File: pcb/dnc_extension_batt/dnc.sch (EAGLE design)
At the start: 49 parts, among them Q1 IRF9321PBF, Q2 IRF9321PBF, Q5 BSS138

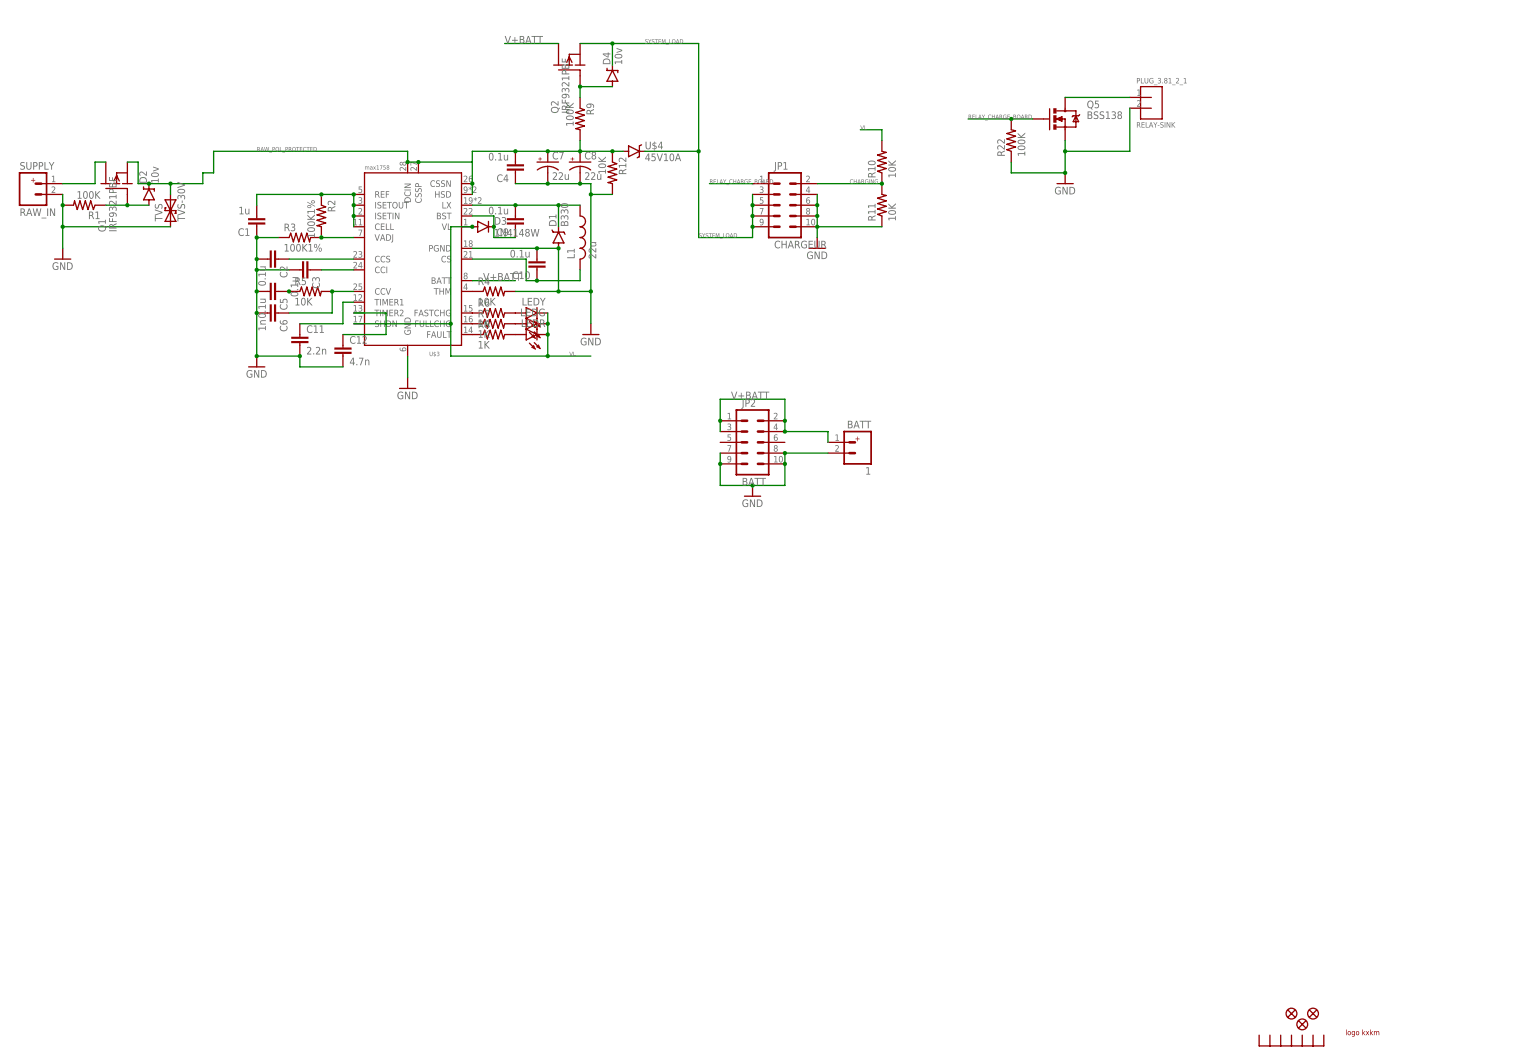
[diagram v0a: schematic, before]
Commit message: add remote + enclosure
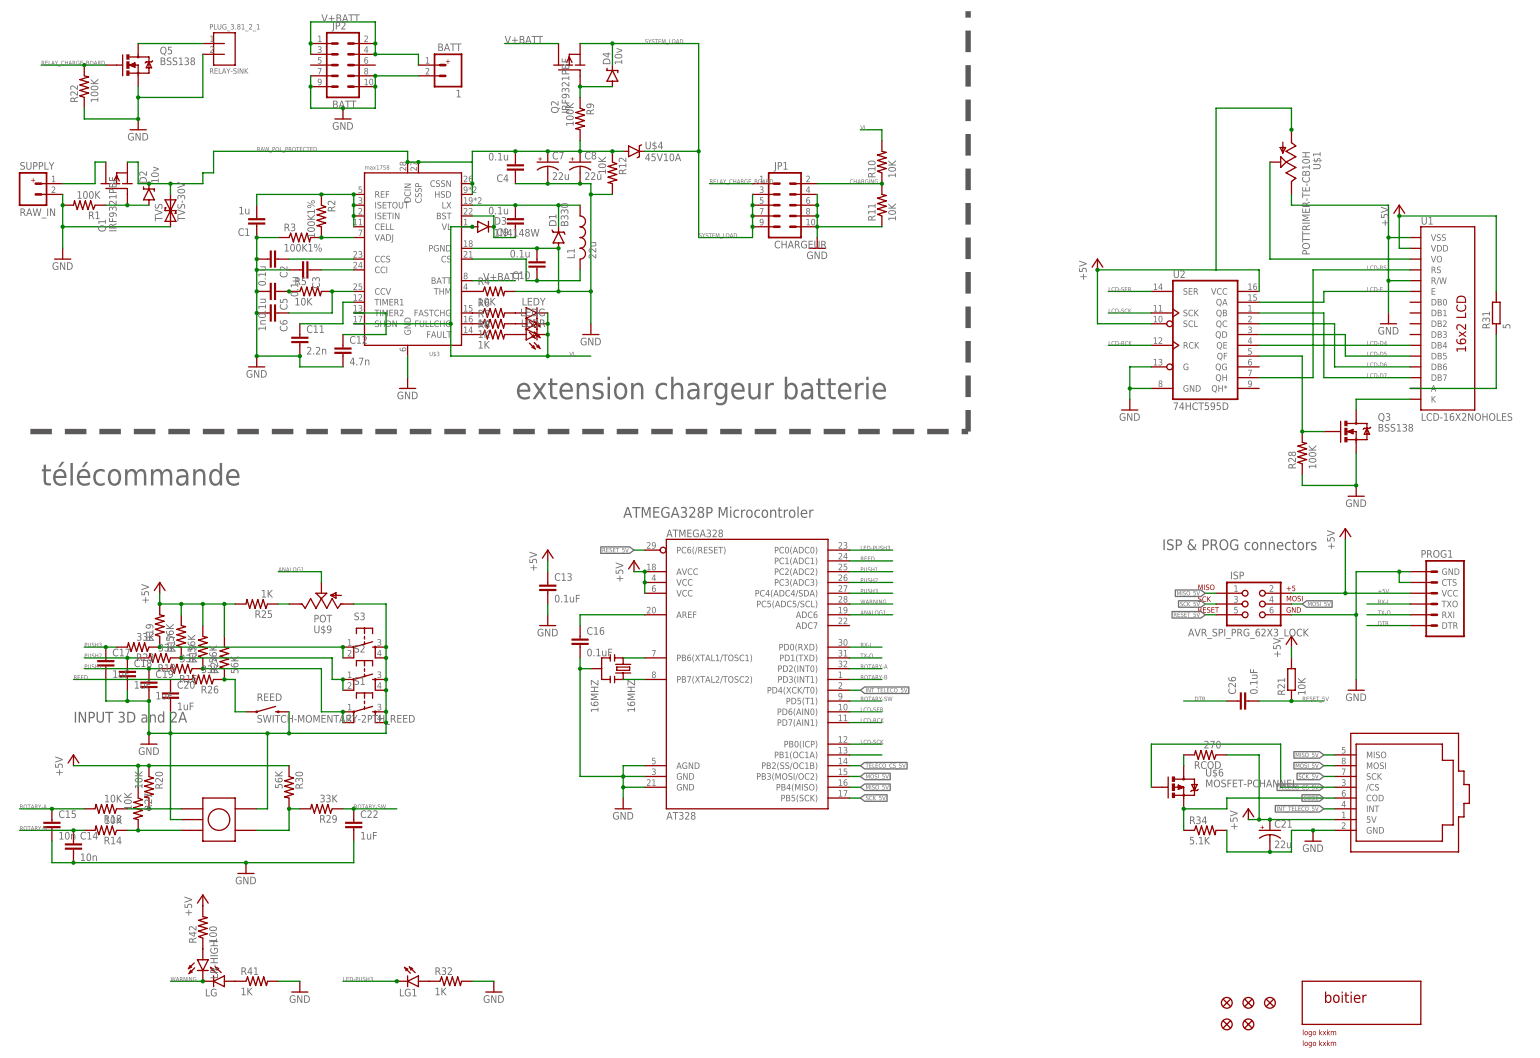
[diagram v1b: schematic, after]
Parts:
- added 16MHZ: 16MHZ, SparkFun-FreqCtrl:RESONATOR16MHZ
- added AT328: ATMEGA328, SparkFun:ATMEGA168
- added C13, C16, C26: 0.1uF, rcl:C-EUC0603
- added C14, C15: 10n, rcl:C-EUC0603
- added C17, C18, C19, C20, C22: 1uF, rcl:C-EUC0603
- added C21: 22u, SparkFun-Passives:CAP_POL1206
- added ISP: AVR_SPI_PRG_62X3_LOCK, SparkFun:AVR_SPI_PRG_62X3_LOCK
- added JP3, JP4: FIDUCIAL1X2.5, SparkFun:FIDUCIAL1X2.5
- added LG, LG1, LR-HIGH: (no value), SparkFun-LED:LED1206
- added PROG1: (no value), SparkFun:ARDUINO_SERIAL_PROGRAMLOCK
- added Q3: BSS138, SparkFun-DiscreteSemi:MOSFET-NCHANNELBSS138
- added R13, R14, R20, R27: 10K, SparkFun-Passives:RESISTOR0603-RES
- added R15, R17, R19, R24, R30: 56K, SparkFun-Passives:RESISTOR0603-RES
- added R16, R18, R23, R26, R29: 33K, SparkFun-Passives:RESISTOR0603-RES
- added R21: 10K, rcl:R-EU_R0603
- added R25, R32, R41: 1K, SparkFun-Passives:RESISTOR0603-RES
- added R28: 100K, SparkFun-Passives:RESISTOR0603-RES
- added R31: 5, rcl:R-EU_R0603
- added R34: 5.1K, SparkFun-Passives:RESISTOR0603-RES
- added R42: 100, SparkFun-Passives:RESISTOR0603-RES
- added RCOD: 270, SparkFun-Passives:RESISTOR0603-RES
- added REED: SWITCH-MOMENTARY-2PTH_REED, SparkFun-Electromechanical:SWITCH-MOMENTARY-2PTH_REED
- added S1, S2, S3: (no value), SparkFun:TAC_SWITCHPTH
- added U$5: BOITIERBOITIER_FARNELLE_479-0020-0, pierre_vv:BOITIERBOITIER_FARNELLE_479-0020-0
- added U$6: MOSFET-PCHANNEL, SparkFun-DiscreteSemi:MOSFET-PCHANNEL
- added U$6MOV: LOGO, pierre_vv:LOGO
- added U$7: ROTARYEC12D1564404, pierre_vv:ROTARYEC12D1564404
- added U$8: RJ45-EXTDNC, con-amphenol-rj45-ld:RJ45-EXTDNC
- added U$9: POT, pierre_vv:POT
- added U1: LCD-16X2NOHOLES, SparkFun-Displays:LCD-16X2NOHOLES
- added U2: 74HCT595D, IC:74HCT595D
- U$1: value RADIATEUR -> POTTRIMER-TE-CB10H; device pierre_vv:RADIATEUR -> pierre_vv:POTTRIMER-TE-CB10H
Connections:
- new net +5V: AT328.AVCC, AT328.VCC@1, AT328.VCC@2, C13.1, C21.+, ISP.2, PROG1.VCC, R15.2, R17.2, R19.2, R20.1, R21.2, R24.2, R25.2, R27.1, R30.1, R31.2, R42.2, RCOD.1, U$1.A, U$8.5V, U1.VDD, U2.SCL, U2.VCC
- new net ANALOG1: AT328.ADC6, U$9.S
- new net AREF: AT328.AREF, C16.1
- new net CODE: R34.1, U$6.S, U$8.COD
- new net DTR: C26.1, PROG1.DTR
- new net INT_TELECO_5V: AT328.PD4(XCK/T0), U$8.INT
- new net LCD-D4: U1.DB4, U2.QE
- new net LCD-D5: U1.DB5, U2.QD
- new net LCD-D6: U1.DB6, U2.QC
- new net LCD-D7: U1.DB7, U2.QB
- new net LCD-E: U1.E, U2.QA
- new net LCD-LED-CONTROL: Q3.G, R28.2, U2.QF
- new net LCD-RCK: AT328.PD7(AIN1), U2.RCK
- new net LCD-RS: U1.RS, U2.QH
- new net LCD-SCK: AT328.PB0(ICP), U2.SCK
- new net LCD-SER: AT328.PD6(AIN0), U2.SER
- new net LED-PUSH3: AT328.PC0(ADC0), LG1.C
- new net MISO_5V: AT328.PB4(MISO), ISP.1, U$8.MISO
- new net MOSI_5V: AT328.PB3(MOSI/OC2), ISP.4, U$8.MOSI
- new net N$22: R15.1, R16.1, S1.1, S1.2
- new net N$23: R14.1, R27.2, U$7.A
- new net N$24: R17.1, R18.1, S2.1, S2.2
- new net N$25: R13.1, R20.2, U$7.B
- new net N$26: R19.1, R23.1, S3.1, S3.2
- new net N$27: R25.1, U$9.E
- new net N$28: R24.1, R26.1, REED.1
- new net N$29: LR-HIGH.A, R42.1
- new net N$30: LG.A, R41.1
- new net N$31: R29.2, R30.2, U$7.SW2
- new net N$32: R31.1, U1.A
- new net N$33: U$1.S, U1.VO
- new net N$34: Q3.D, U1.K
- new net N$35: LG1.A, R32.1
- new net N$36: RCOD.2, U$6.D
- new net N$38: AT328.PB1(OC1A)
- new net N$43: 16MHZ.1, AT328.PB6(XTAL1/TOSC1)
- new net N$44: 16MHZ.3, AT328.PB7(XTAL2/TOSC2)
- new net PUSH1: AT328.PC2(ADC2), C19.1, R16.2
- new net PUSH2: AT328.PC3(ADC3), C18.1, R18.2
- new net PUSH3: AT328.PC4(ADC4/SDA), C17.1, R23.2
- new net REED: AT328.PC1(ADC1), C20.1, R26.2
- new net RESET_5V: AT328.PC6(/RESET), C26.2, ISP.5, R21.1
- new net ROTARY-A: AT328.PD2(INT0), C15.1, R13.2
- new net ROTARY-B: AT328.PD3(INT1), C14.1, R14.2
- new net ROTARY-SW: AT328.PD5(T1), C22.1, R29.1
- new net RX-I: AT328.PD0(RXD), PROG1.TXO
- new net SCK_5V: AT328.PB5(SCK), ISP.3, U$8.SCK
- new net TELECO_CS_5V: AT328.PB2(SS/OC1B), U$6.G, U$8./CS
- new net TX-O: AT328.PD1(TXD), PROG1.RXI
- new net WARNING: AT328.PC5(ADC5/SCL), LG.C, LR-HIGH.C
- net GND: now also 16MHZ.2, AT328.AGND, AT328.GND@1, AT328.GND@2, C13.2, C14.2, C15.2, C16.2, C17.2, C18.2, C19.2, C20.2, C21.-, C22.2, ISP.6, PROG1.CTS, PROG1.GND, Q3.S, R28.1, R32.2, R34.2, R41.2, REED.2, S1.3, S1.4, S2.3, S2.4, S3.3, S3.4, U$1.E, U$7.COM, U$7.SW1, U$8.GND, U$9.A, U1.R/W, U1.VSS, U2.G, U2.GND
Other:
- note added: "ATMEGA328P Microcontroler"
- note added: "CS titreur driver"
- note added: "INPUT 3D and 2A"
- note added: "ISP & PROG connectors"
- note added: "extension chargeur batterie"
- note added: "télécommande"
- moved on the sheet: 1, JP2, PLUG_3.81_2_1, Q5, R22

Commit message: BOM ext teleco et chargeur
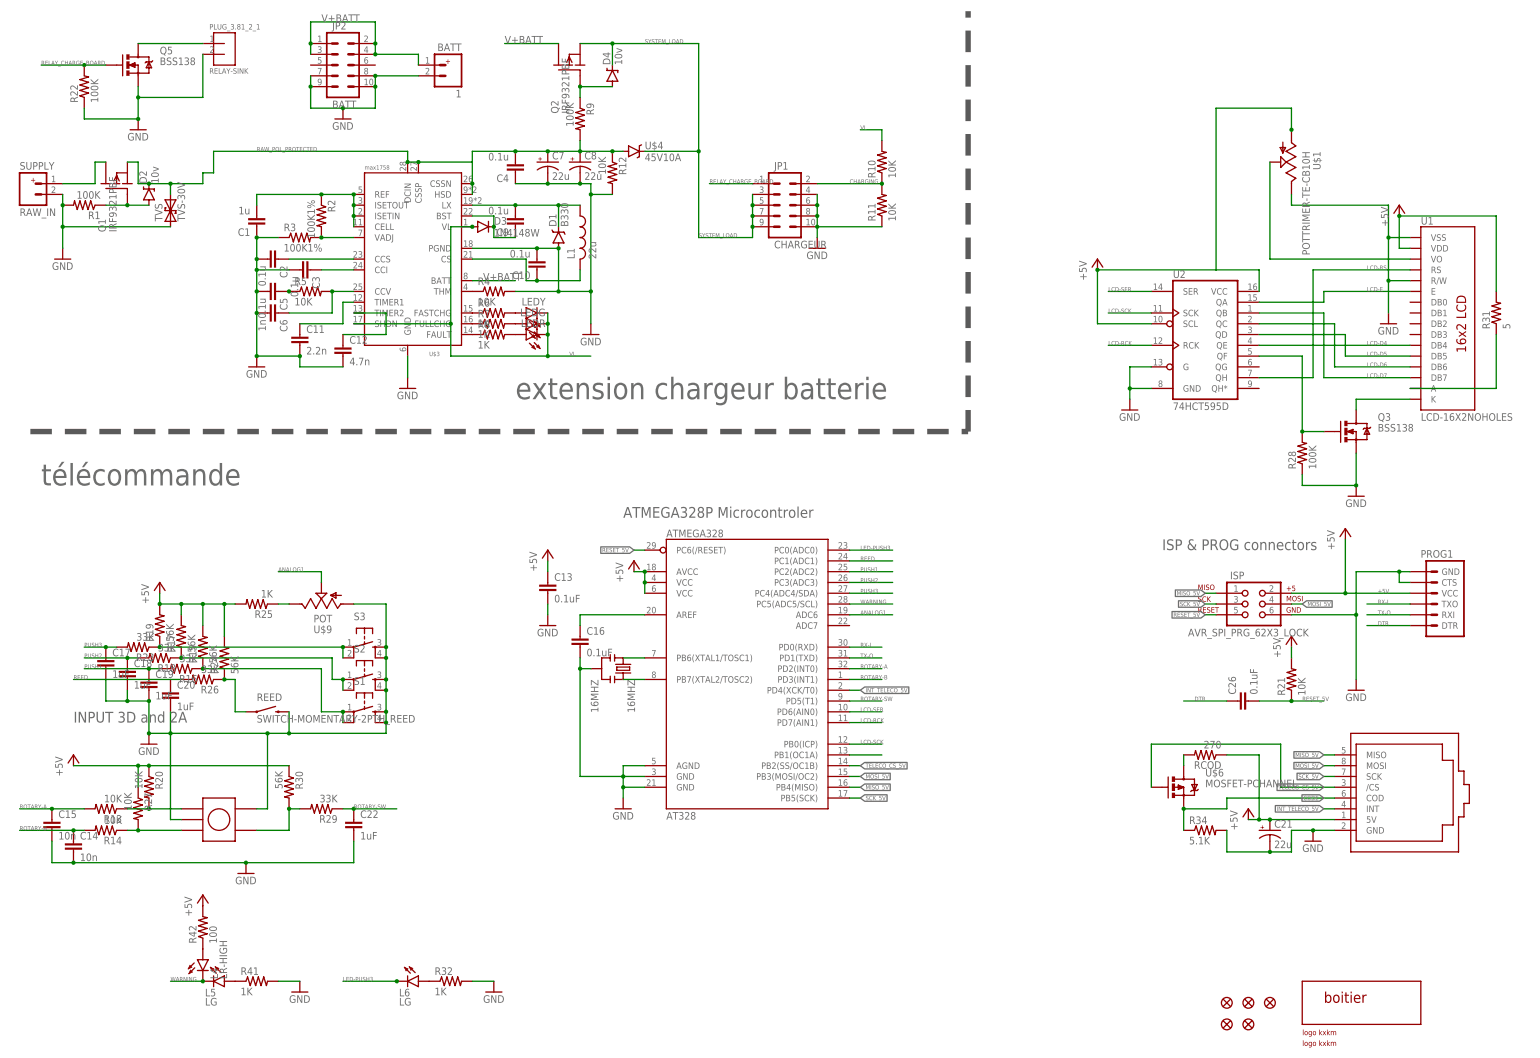
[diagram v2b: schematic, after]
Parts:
- 1, C1, C11, C12, C2, C3, C5, C6, D1, D2, D3, D4, JP1, JP2, L1, LEDG, LEDR, LEDY, PLUG_3.81_2_1, Q1, Q2, Q5, R1, R10, R11, R12, R2, R22, R3, R4, R5, R6, R7, R8, R9, RAW_IN, TVS, U$3, U$4: C (none) -> 1
- C10, C4, C7, C8, C9: C (none) -> 1; VMIN (none) -> 35V
- L4: value (none) -> LR-HIGH
- L5, L6: value (none) -> LG
- R21: device rcl:R-EU_R0603 -> SparkFun-Passives:RESISTOR0603-RES
- R31: device rcl:R-EU_R0603 -> SparkFun-Passives:RESISTOR0805-RES; P (none) -> 250mw
- renumbered LG to L5, LG1 to L6, LR-HIGH to L4

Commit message: major change correction : - driver led position - add usb for power - correct max 202 voltage problem - titrer connector position - forget line - power trace consideration
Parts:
- JP1: device SparkFun:M05X2SHD_LOCK -> pierre_vv:M05X2
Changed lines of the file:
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@@
 <grid distance="0.1" unitdist="inch" unit="inch" style="lines" multiple="1" display="no" altdistance="0.01" altunitdist="inch" altunit="inch"/>
 <layers>
-<layer number="1" name="Top" color="4" fill="1" visible="yes" active="no"/>
-<layer number="16" name="Bottom" color="1" fill="1" visible="yes" active="no"/>
-<layer number="17" name="Pads" color="2" fill="1" visible="yes" active="no"/>
-<layer number="18" name="Vias" color="2" fill="1" visible="yes" active="no"/>
-<layer number="19" name="Unrouted" color="13" fill="1" visible="yes" active="no"/>
-<layer number="20" name="Dimension" color="15" fill="1" visible="yes" active="no"/>
-<layer number="21" name="tPlace" color="7" fill="1" visible="yes" active="no"/>
-<layer number="22" name="bPlace" color="7" fill="1" visible="yes" active="no"/>
-<layer number="23" name="tOrigins" color="15" fill="1" visible="yes" active="no"/>
-<layer number="24" name="bOrigins" color="15" fill="1" visible="yes" active="no"/>
-<layer number="25" name="tNames" color="7" fill="1" visible="yes" active="no"/>
-<layer number="26" name="bNames" color="7" fill="1" visible="yes" active="no"/>
-<layer number="27" name="tValues" color="7" fill="1" visible="yes" active="no"/>
-<layer number="28" name="bValues" color="7" fill="1" visible="yes" active="no"/>
+<layer number="1" name="Top" color="4" fill="1" visible="no" active="no"/>
+<layer number="16" name="Bottom" color="1" fill="1" visible="no" active="no"/>
+<layer number="17" name="Pads" color="2" fill="1" visible="no" active="no"/>
+<layer number="18" name="Vias" color="2" fill="1" visible="no" active="no"/>
+<layer number="19" name="Unrouted" color="13" fill="1" visible="no" active="no"/>
+<layer number="20" name="Dimension" color="15" fill="1" visible="no" active="no"/>
+<layer number="21" name="tPlace" color="7" fill="1" visible="no" active="no"/>
+<layer number="22" name="bPlace" color="7" fill="1" visible="no" active="no"/>
+<layer number="23" name="tOrigins" color="15" fill="1" visible="no" active="no"/>
+<layer number="24" name="bOrigins" color="15" fill="1" visible="no" active="no"/>
+<layer number="25" name="tNames" color="7" fill="1" visible="no" active="no"/>
+<layer number="26" name="bNames" color="7" fill="1" visible="no" active="no"/>
+<layer number="27" name="tValues" color="7" fill="1" visible="no" active="no"/>
+<layer number="28" name="bValues" color="7" fill="1" visible="no" active="no"/>
 <layer number="29" name="tStop" color="7" fill="3" visible="no" active="no"/>
 <layer number="30" name="bStop" color="7" fill="6" visible="no" active="no"/>
@@
 <layer number="35" name="tGlue" color="7" fill="4" visible="no" active="no"/>
 <layer number="36" name="bGlue" color="7" fill="5" visible="no" active="no"/>
-<layer number="37" name="tTest" color="7" fill="1" visible="yes" active="no"/>
-<layer number="38" name="bTest" color="7" fill="1" visible="yes" active="no"/>
+<layer number="37" name="tTest" color="7" fill="1" visible="no" active="no"/>
+<layer number="38" name="bTest" color="7" fill="1" visible="no" active="no"/>
 <layer number="39" name="tKeepout" color="4" fill="11" visible="no" active="no"/>
 <layer number="40" name="bKeepout" color="1" fill="11" visible="no" active="no"/>
@@
 <layer number="44" name="Drills" color="7" fill="1" visible="no" active="no"/>
 <layer number="45" name="Holes" color="7" fill="1" visible="no" active="no"/>
-<layer number="46" name="Milling" color="3" fill="1" visible="yes" active="no"/>
-<layer number="47" name="Measures" color="7" fill="1" visible="yes" active="no"/>
-<layer number="48" name="Document" color="7" fill="1" visible="yes" active="no"/>
-<layer number="49" name="Reference" color="7" fill="1" visible="yes" active="no"/>
-<layer number="50" name="dxf" color="7" fill="1" visible="yes" active="no"/>
-<layer number="51" name="tDocu" color="14" fill="1" visible="yes" active="no"/>
-<layer number="52" name="bDocu" color="14" fill="1" visible="yes" active="no"/>
-<layer number="53" name="tGND_GNDA" color="7" fill="9" visible="yes" active="no"/>
-<layer number="54" name="bGND_GNDA" color="1" fill="9" visible="yes" active="no"/>
-<layer number="56" name="wert" color="7" fill="1" visible="yes" active="no"/>
-<layer number="57" name="tCAD" color="7" fill="1" visible="yes" active="no"/>
+<layer number="46" name="Milling" color="3" fill="1" visible="no" active="no"/>
+<layer number="47" name="Measures" color="7" fill="1" visible="no" active="no"/>
+<layer number="48" name="Document" color="7" fill="1" visible="no" active="no"/>
+<layer number="49" name="Reference" color="7" fill="1" visible="no" active="no"/>
+<layer number="50" name="dxf" color="7" fill="1" visible="no" active="no"/>
+<layer number="51" name="tDocu" color="14" fill="1" visible="no" active="no"/>
+<layer number="52" name="bDocu" color="14" fill="1" visible="no" active="no"/>
+<layer number="53" name="tGND_GNDA" color="7" fill="9" visible="no" active="no"/>
+<layer number="54" name="bGND_GNDA" color="1" fill="9" visible="no" active="no"/>
+<layer number="56" name="wert" color="7" fill="1" visible="no" active="no"/>
+<layer number="57" name="tCAD" color="7" fill="1" visible="no" active="no"/>
 <layer number="90" name="Modules" color="5" fill="1" visible="yes" active="yes"/>
 <layer number="91" name="Nets" color="2" fill="1" visible="yes" active="yes"/>
@@
 <part name="JP14" library="SparkFun" deviceset="FIDUCIAL" device="1X2.5"/>
 <part name="JP19" library="SparkFun" deviceset="FIDUCIAL" device="1X2.5"/>
-<part name="JP1" library="SparkFun" deviceset="M05X2" device="SHD_LOCK" value="CHARGEUR">
+<part name="JP1" library="pierre_vv" deviceset="M05X2" device="" value="CHARGEUR">
 <attribute name="C" value="1"/>
 </part>
